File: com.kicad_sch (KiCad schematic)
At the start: 0 parts

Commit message: Added COM Radio sheet
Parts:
- added AE?: Antenna, symbol Device:Antenna
- added J?: HeadPhone 2, symbol Connector:AudioJack2_Ground
- added J?: RF Output (TNC), symbol Connector_Generic:Conn_01x01
- added J?: HeadPhone 1, symbol Connector:AudioJack2_Ground
- added J?: DB15_Male, symbol Connector:DB15_Male
- added J?: PL?-B, symbol Connector:Conn_01x02_Female
- added J?: PL1-B, symbol Connector:Conn_01x02_Female
- added J?: PL?-B, symbol Connector:Conn_01x02_Male
- added J?: MIC 1, symbol Connector:AudioJack2_Ground
- added J?: PL1-A, symbol Connector:Conn_01x02_Male
- added J?: PL?-A, symbol Connector:Conn_01x02_Male
- added J?: PL?-A, symbol Connector:Conn_01x02_Female
- added J?: DB25_Female, symbol Connector:DB25_Female
- added J?: MIC 2, symbol Connector:AudioJack2_Ground
- added J?: DB15_Female, symbol Connector:DB15_Female
- added J?: DB25_Male, symbol Connector:DB25_Male
- added SW? (x2): PTT 2, symbol Switch:SW_Push
- added SW?: Intercom Enable, symbol Switch:SW_SPST
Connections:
- new net: J?.10, J?.G, J?.G
- new net: J?.11, J?.S, J?.S
- new net: AE?.1 (A), J?.1 (Pin_1)
- new net: J?.2, J?.3
- new net: J?.3, J?.4
- new net: J?.13, J?.8
- new net: J?.12, J?.9 (P9)
- new net: J?.1 (Pin_1), J?.S
- new net: J?.2 (Pin_2), J?.2 (Pin_2), J?.22 (P22), J?.G, J?.G, SW?.2 (B)
- new net: J?.1 (Pin_1), SW?.1 (x2)
- new net: J?.2 (Pin_2), SW?.2 (x2)
- new net: J?.1 (Pin_1), J?.23 (P23), J?.S
- new net: J?.15 (P15), J?.T
- new net: J?.14 (P14), J?.T
- new net: J?.17 (P17), SW?.1 (A)
- new net +12v COM Radio: J?.1 (Pin_1), J?.24 (P24), J?.25 (P25)
- new net 0v COM Radio: J?.1, J?.19 (P19), J?.2 (Pin_2), J?.4, J?.9
- new net ECB Output 1: J?.1 (Pin_1)
- new net Ground Bus TB6/1: J?.2 (Pin_2)
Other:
- note added: "Aux In"
- note added: "DC Power"
- note added: "Ground"
- note added: "Intercom PTT"
- note added: "MIC 1 In"
- note added: "MIC 2 In"
- note added: "MIC Ground"
- note added: "PTT 1"
- note added: "PTT 2"
- note added: "Phone Ground"
- note added: "Phone Out"
- note added: "Power In"
- note added: "Power On"
- note added: "Remote On"
- note added: "TC90 Controller"
- note added: "TC90 Power"
- note added: "TMAP 1A"
- note added: "TMAP 1B"
- note added: "TMAP A"
- note added: "TMAP B"
- note added: "TY91 COM Radio"

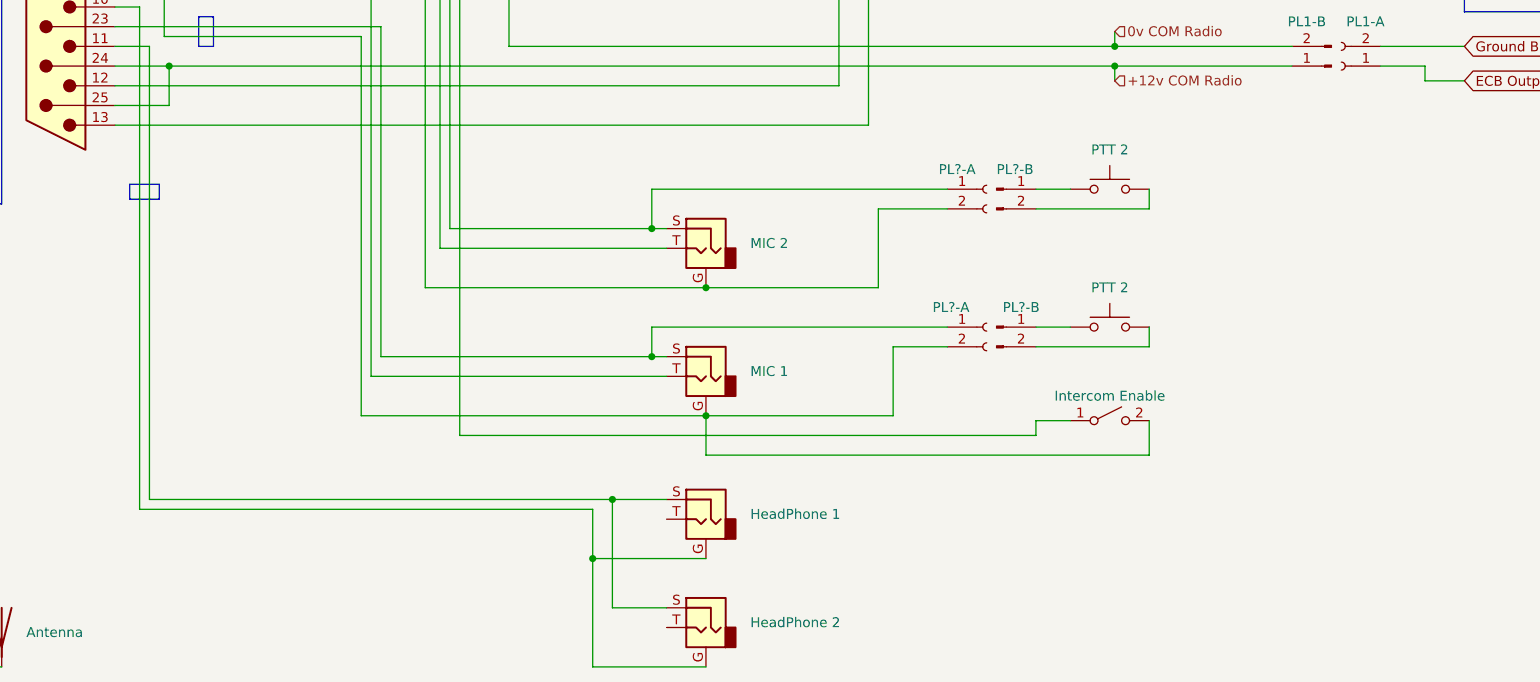
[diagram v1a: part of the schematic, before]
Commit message: Added Connectors sheet
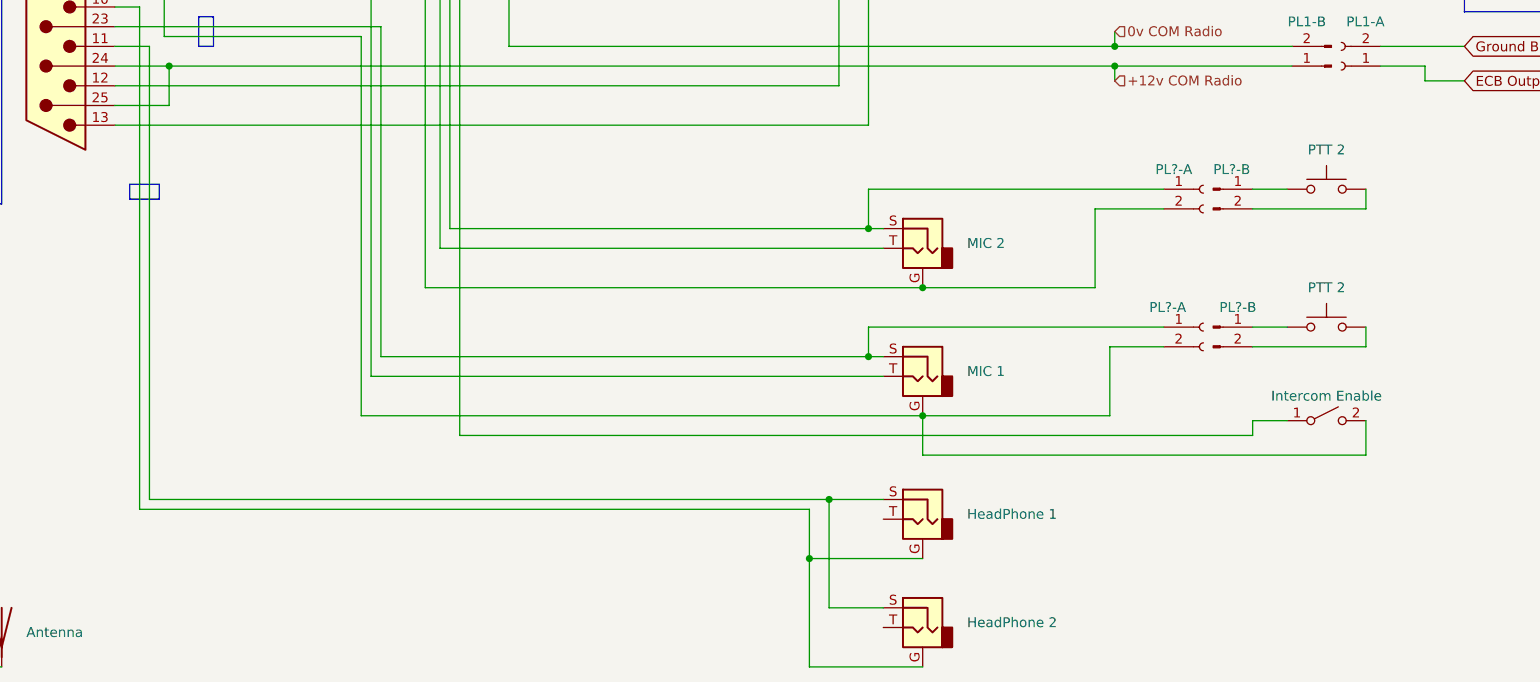
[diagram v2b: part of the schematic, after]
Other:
- title: (none) -> Europa COM Radio

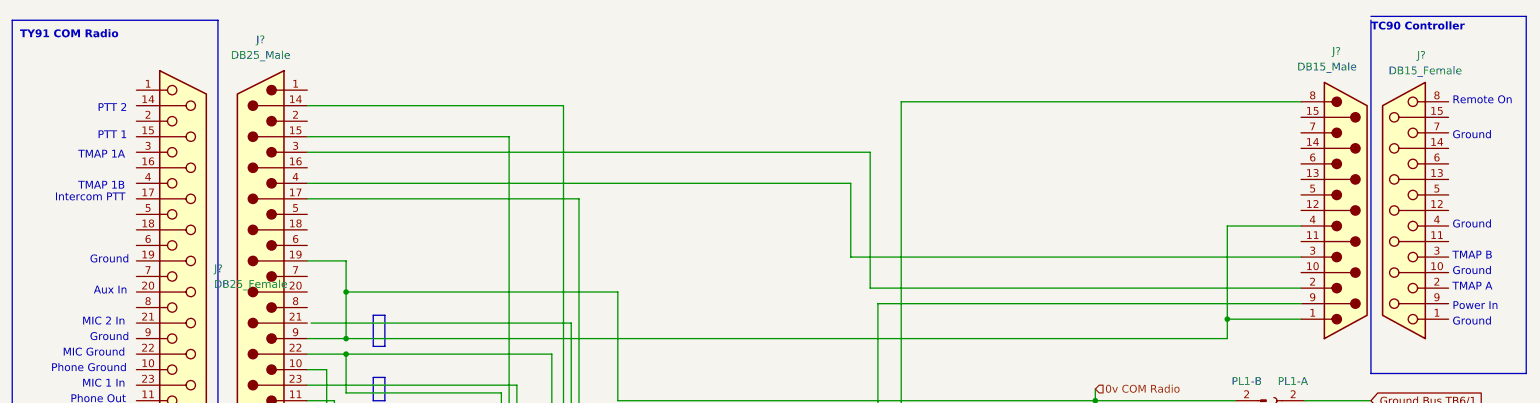
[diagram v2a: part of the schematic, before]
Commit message: Small updates to multiple sheets, and major update to SmartAss sheet
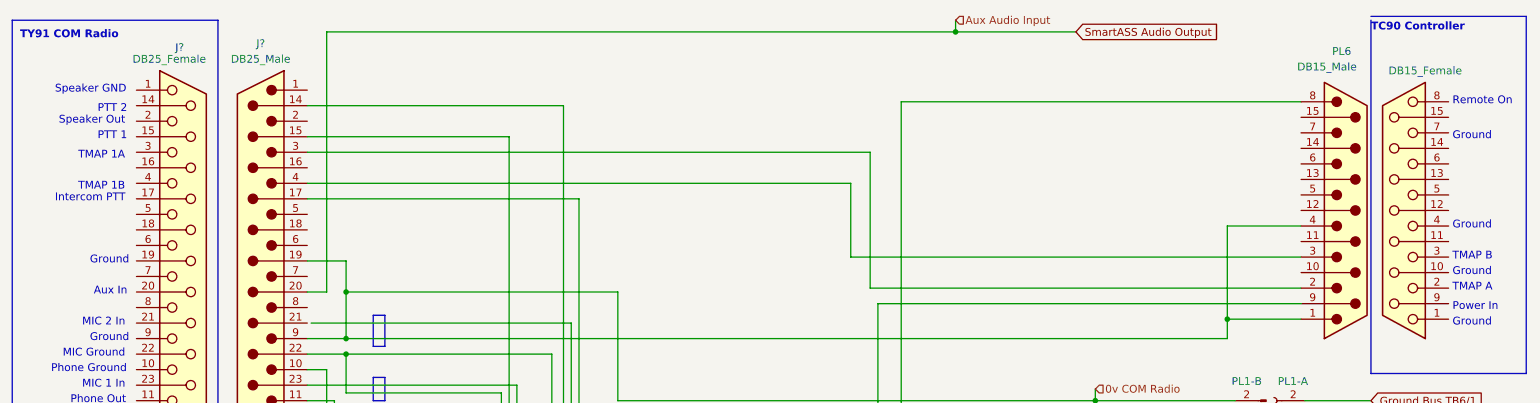
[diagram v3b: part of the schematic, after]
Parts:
- gave numbers to parts that had none: 1
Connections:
- net SmartASS Audio Output: now reaches J?.20 (P20)
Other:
- note added: "Speaker GND"
- note added: "Speaker Out"
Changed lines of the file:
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@@
   (title_block
     (title "Europa COM Radio")
-    (date "2022-12-26")
-    (rev "1")
+    (date "2022-12-29")
+    (rev "2")
   )
   (junction (at 197.485 80.645) (diameter 0) (color 0 0 0 0)
   )
+  (junction (at 174.625 20.32) (diameter 0) (color 0 0 0 0)
+  )
   (junction (at 75.565 83.185) (diameter 0) (color 0 0 0 0)
   )
@@
     (stroke (width 0) (type default) (color 0 0 0 0))
   )
+  (wire (pts (xy 71.755 62.865) (xy 71.755 20.32))
+    (stroke (width 0) (type default) (color 0 0 0 0))
+  )
   (polyline (pts (xy 81.28 71.755) (xy 81.28 66.675))
     (stroke (width 0) (type default) (color 0 0 0 0))
@@
     (stroke (width 0) (type default) (color 0 0 0 0))
   )
+  (wire (pts (xy 71.755 20.32) (xy 174.625 20.32))
+    (stroke (width 0) (type default) (color 0 0 0 0))
+  )
   (wire (pts (xy 215.265 119.38) (xy 229.87 119.38))
     (stroke (width 0) (type default) (color 0 0 0 0))
@@
     (stroke (width 0) (type default) (color 0 0 0 0))
   )
+  (wire (pts (xy 68.58 62.865) (xy 71.755 62.865))
+    (stroke (width 0) (type default) (color 0 0 0 0))
+  )
   (wire (pts (xy 108.585 111.76) (xy 172.72 111.76))
     (stroke (width 0) (type default) (color 0 0 0 0))
@@
     (stroke (width 0) (type default) (color 0 0 0 0))
   )
+  (wire (pts (xy 174.625 20.32) (xy 194.31 20.32))
+    (stroke (width 0) (type default) (color 0 0 0 0))
+  )
   (wire (pts (xy 165.735 104.14) (xy 165.735 99.06))
     (stroke (width 0) (type default) (color 0 0 0 0))
@@
     (stroke (width 0) (type default) (color 0 0 0 0))
   )
+  (wire (pts (xy 174.625 18.415) (xy 174.625 20.32))
+    (stroke (width 0) (type default) (color 0 0 0 0))
+  )
   (wire (pts (xy 68.58 88.265) (xy 75.565 88.265))
     (stroke (width 0) (type default) (color 0 0 0 0))
@@
   )
   (text "Ground" (at 255.905 52.705 0)
+    (effects (font (size 1.27 1.27)) (justify left bottom))
+  )
+  (text "Speaker Out" (at 27.94 35.56 0)
     (effects (font (size 1.27 1.27)) (justify left bottom))
   )
@@
   )
   (text "Ground" (at 255.905 60.325 0)
+    (effects (font (size 1.27 1.27)) (justify left bottom))
+  )
+  (text "Speaker GND" (at 27.305 30.48 0)
     (effects (font (size 1.27 1.27)) (justify left bottom))
   )
@@
     )
   )
+  (global_label "SmartASS Audio Output" (shape input) (at 194.31 20.32 0) (fields_autoplaced)
+    (effects (font (size 1.27 1.27)) (justify left))
+    (property "Intersheet References" "${INTERSHEET_REFS}" (id 0) (at 219.0993 20.2406 0)
+      (effects (font (size 1.27 1.27)) (justify left) hide)
+    )
+  )
+  (hierarchical_label "Aux Audio Input" (shape input) (at 174.625 18.415 0)
+    (effects (font (size 1.27 1.27)) (justify left))
+  )
   (hierarchical_label "0v COM Radio" (shape input) (at 197.485 78.74 0)
     (effects (font (size 1.27 1.27)) (justify left))
@@
   (symbol (lib_id "Connector:DB15_Male") (at 238.76 49.53 0) (unit 1)
     (in_bom yes) (on_board yes)
-    (property "Reference" "J?" (id 0) (at 236.22 23.495 0)
+    (property "Reference" "PL6" (id 0) (at 236.22 23.495 0)
       (effects (font (size 1.27 1.27)) (justify left))
     )
@@
   )
   (symbol (lib_id "Connector:DB25_Female") (at 48.26 60.325 0) (unit 1)
-    (in_bom yes) (on_board yes) (fields_autoplaced)
-    (property "Reference" "J?" (id 0) (at 53.34 59.0549 0)
+    (in_bom yes) (on_board yes)
+    (property "Reference" "J?" (id 0) (at 46.99 22.86 0)
       (effects (font (size 1.27 1.27)) (justify left))
     )
-    (property "Value" "DB25_Female" (id 1) (at 53.34 61.5949 0)
+    (property "Value" "DB25_Female" (id 1) (at 40.005 24.765 0)
       (effects (font (size 1.27 1.27)) (justify left))
     )
@@
   (symbol (lib_id "Connector:DB15_Female") (at 247.65 49.53 180) (unit 1)
     (in_bom yes) (on_board yes)
-    (property "Reference" "J?" (id 0) (at 250.825 24.13 0))
+    (property "Reference" "J?" (id 0) (at 250.825 24.13 0)
+      (effects (font (size 1.27 1.27)) hide)
+    )
     (property "Value" "DB15_Female" (id 1) (at 251.46 26.67 0))
     (property "Footprint" "" (id 2) (at 247.65 49.53 0)
@@
   )
   (symbol (lib_id "Connector:DB25_Male") (at 60.96 60.325 180) (unit 1)
-    (in_bom yes) (on_board yes) (fields_autoplaced)
-    (property "Reference" "J?" (id 0) (at 60.96 21.59 0))
-    (property "Value" "DB25_Male" (id 1) (at 60.96 24.13 0))
+    (in_bom yes) (on_board yes)
+    (property "Reference" "J?" (id 0) (at 60.96 22.225 0))
+    (property "Value" "DB25_Male" (id 1) (at 60.96 24.765 0))
     (property "Footprint" "" (id 2) (at 60.96 60.325 0)
       (effects (font (size 1.27 1.27)) hide)

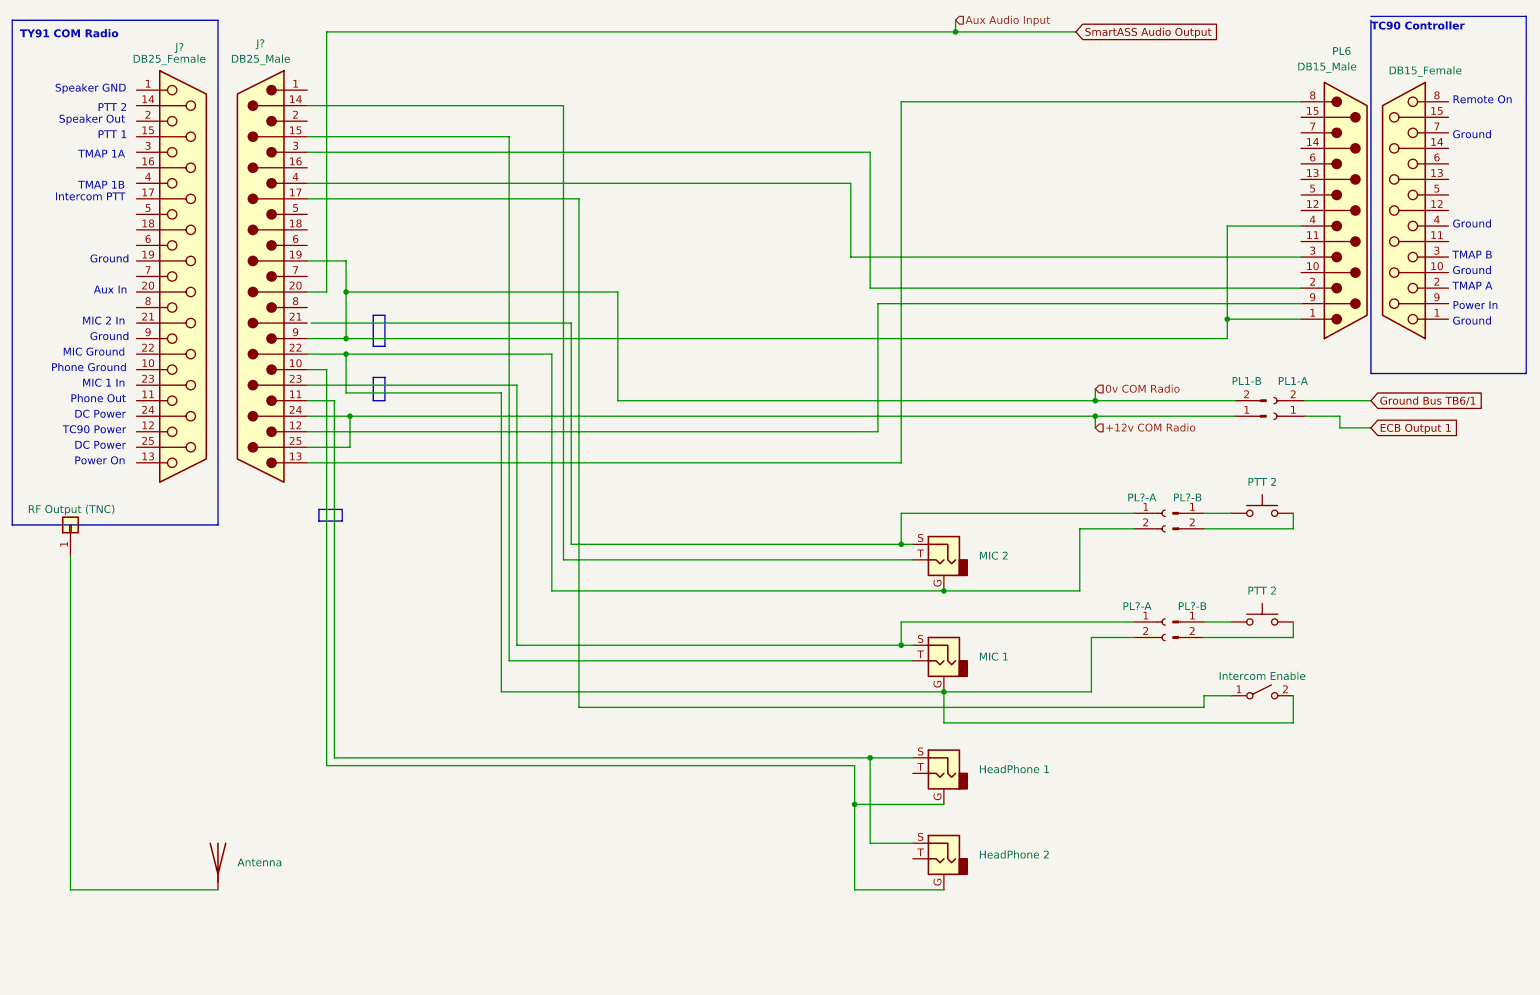
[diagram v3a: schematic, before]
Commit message: Added PL20 to COM Sheet
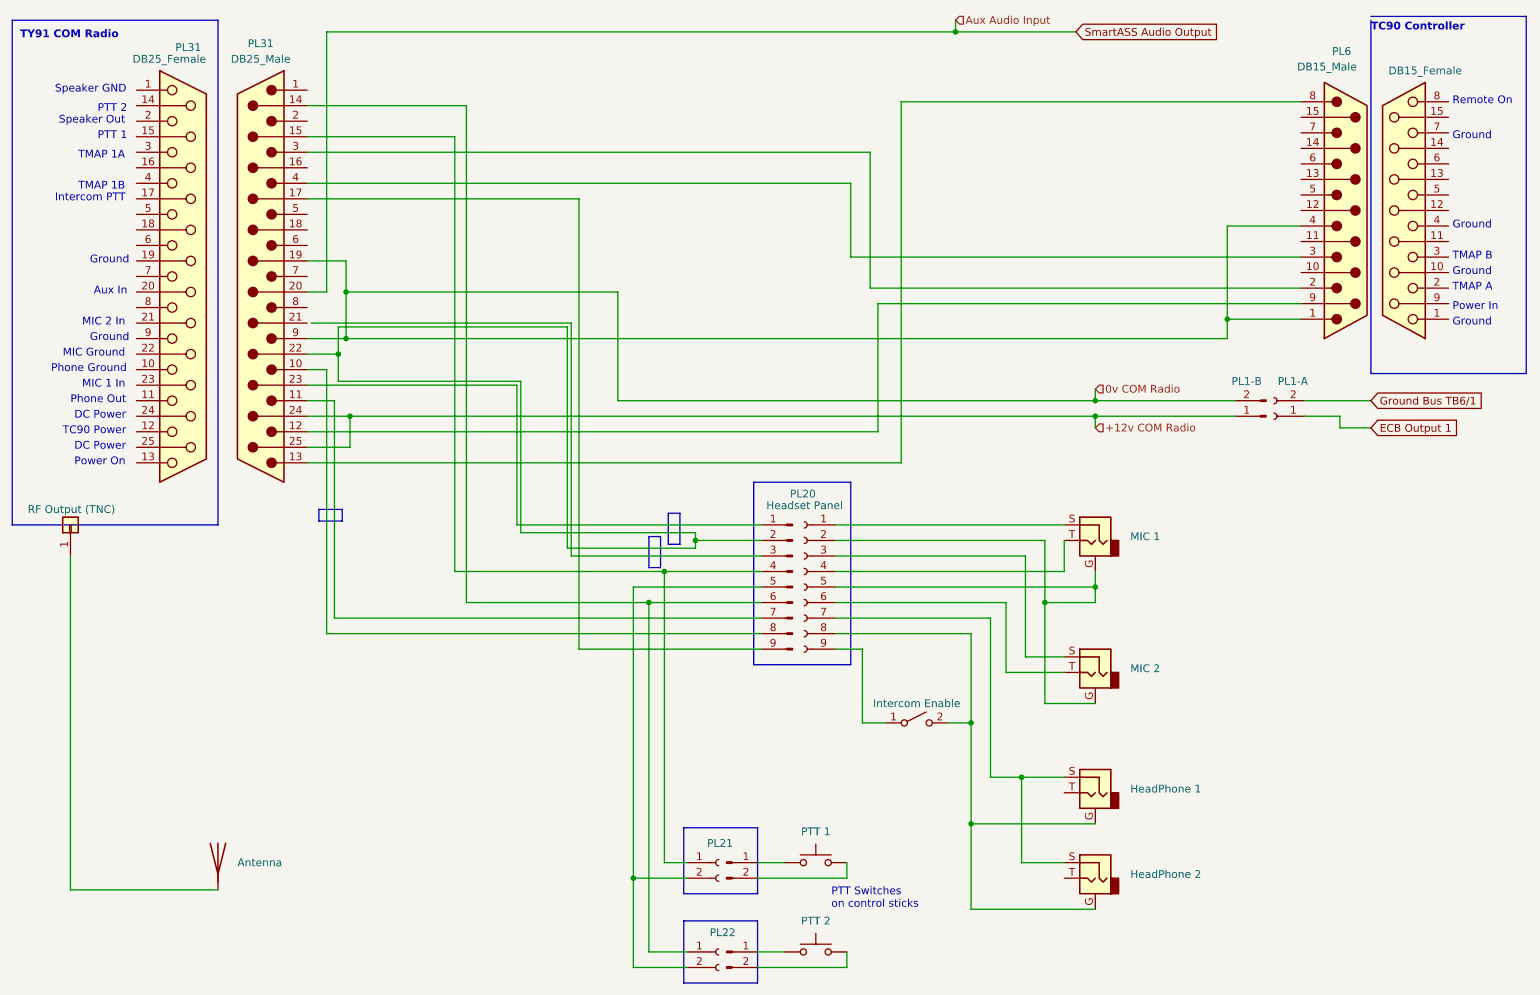
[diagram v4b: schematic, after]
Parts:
- added J?: Conn_01x06_Male, symbol Connector:Conn_01x09_Male
- added PL20: Headset Panel, symbol Connector:Conn_01x09_Female
- J?: value PL?-A -> PL22
- J?: value PL?-A -> PL21
- SW?: value PTT 2 -> PTT 1
- gave numbers to parts that had none: 1
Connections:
- net at J?.G, J?.G: now also SW?.2 (B), PL20.8 (Pin_8); no longer PL31.10
- net at J?.S, J?.S: now also PL20.7 (Pin_7); no longer PL31.11
- net at J?.1 (Pin_1): now also PL31.14 (P14), J?.6 (Pin_6); no longer J?.S
- net at J?.T: now also PL20.4 (Pin_4); no longer PL31.15 (P15)
- net at J?.T: now also PL20.6 (Pin_6); no longer PL31.14 (P14)
- net at PL31.17 (P17): now also J?.9 (Pin_9); no longer SW?.1 (A)
- new net: J?.2 (Pin_2), J?.2 (Pin_2), J?.5 (Pin_5)
- new net: J?.G, J?.G, PL20.2 (Pin_2), PL20.5 (Pin_5)
- new net: J?.S, PL20.1 (Pin_1)
- new net: J?.1 (Pin_1), PL31.23 (P23)
- new net: J?.2 (Pin_2), PL31.22 (P22)
- new net: J?.1 (Pin_1), J?.4 (Pin_4), PL31.15 (P15)
- new net: J?.7 (Pin_7), PL31.11
- new net: J?.8 (Pin_8), PL31.10
- new net: J?.S, PL20.3 (Pin_3)
- new net: PL20.9 (Pin_9), SW?.1 (A)
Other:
- note added: "PTT Switches on control sticks"
- title: Europa COM Radio -> Europa - COM Radio

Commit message: Catchup
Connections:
- net at J?.3 (Pin_3): now also PL31.21 (P21)
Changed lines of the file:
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@@
-    (stroke (width 0) (type default) (color 0 0 0 0))
-  )
-  (wire (pts (xy 69.215 67.945) (xy 111.76 67.945))
     (stroke (width 0) (type default) (color 0 0 0 0))
   )
@@
     (stroke (width 0) (type default) (color 0 0 0 0))
   )
+  (wire (pts (xy 68.58 67.945) (xy 111.76 67.945))
+    (stroke (width 0) (type default) (color 0 0 0 0))
+  )
